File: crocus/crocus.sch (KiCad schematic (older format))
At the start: 49 parts, among them J1 NEIGHBOR1, J2 NEIGHBOR2, J7 BONUS_ROW, P1 RP-SMA, P2 EXPANSION, T1 BALUN, U1 nRF24L01+, U2 PCA9674, Y1 XTAL

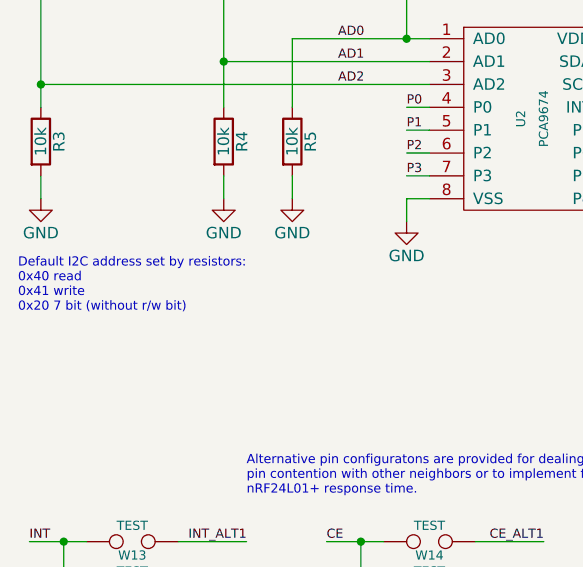
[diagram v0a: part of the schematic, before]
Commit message: standardize on 7-bit format for I2C address documentation
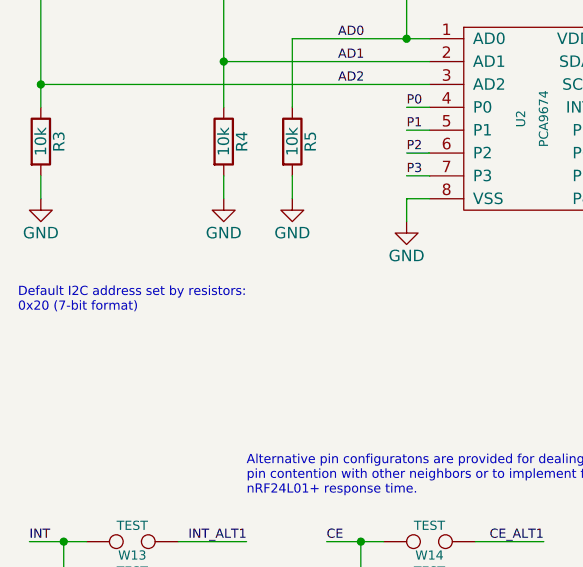
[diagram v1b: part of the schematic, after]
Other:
- note added: "Default I2C address set by resistors:\n0x20 (7-bit format)"
- note removed: "Default I2C address set by resistors:\n0x40 read\n0x41 write\n0x20 7 bit (without r/w bit)"
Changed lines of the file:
@@
 Connection ~ 2500 3050
 Text Notes 800  4250 0    40   ~ 0
-Default I2C address set by resistors:\n0x40 read\n0x41 write\n0x20 7 bit (without r/w bit)
+Default I2C address set by resistors:\n0x20 (7-bit format)
 $Comp
 L GND #PWR036
